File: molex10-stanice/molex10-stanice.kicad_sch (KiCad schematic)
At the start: 19 parts, among them J1 MVE253-5-V, J10 MV132-3.5-V-L, J11 MV132-3.5-V-L, J12 MVE253-5-V, J13 MVE252-5-V, J14 MVE252-5-V, J15 MVE252-5-V, J2 TME 39281103 MOLEX, J3 MVE253-5-V, J4 MVE252-5-V, J5 MVE253-5-V, J6 TME 39281043 MOLEX, J7 RJ12, J8 MV132-3.5-V-L, J9 MV132-3.5-V-L

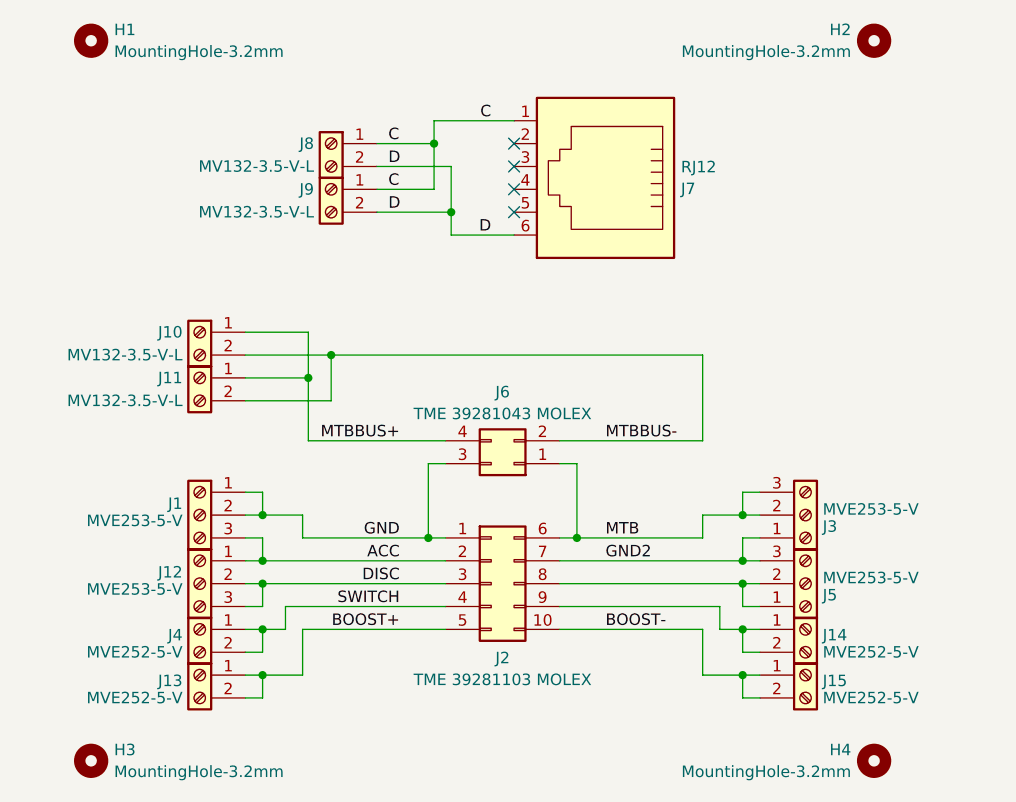
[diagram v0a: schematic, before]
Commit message: molex10-stanice: slight enhancements.
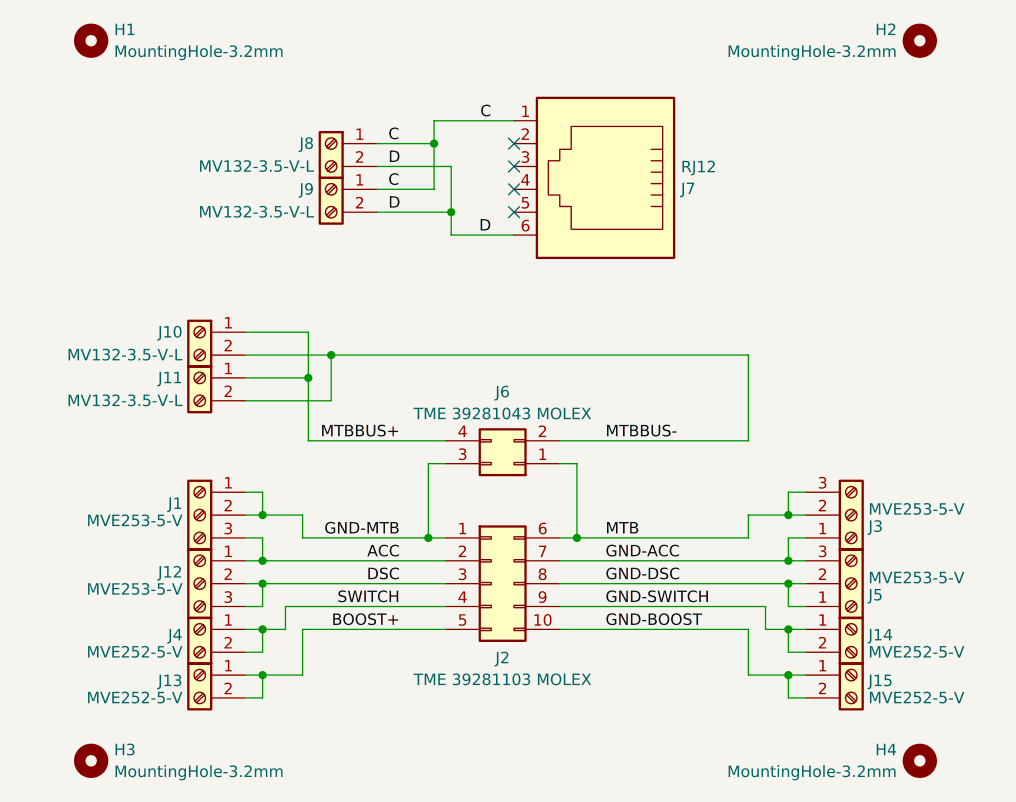
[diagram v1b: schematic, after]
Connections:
- net GND-DSC: now reaches J2.8 (Pin_8), J5.1 (Pin_1), J5.2 (Pin_2)
- net GND-SWITCH: now reaches J14.1 (Pin_1), J14.2 (Pin_2), J2.9 (Pin_9)
- net BOOST- renamed GND-BOOST
- net DISC renamed DSC
- net GND renamed GND-MTB
- net GND2 renamed GND-ACC
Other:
- moved on the sheet: H2, H4, J14, J15, J3, J5
